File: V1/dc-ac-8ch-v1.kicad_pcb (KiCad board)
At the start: 2 copper layers, 98 x 67.8 mm, 103 parts, among them J1 DB142V-5.08-4P, J2 DB142V-5.08-4P, J3 DB142V-5.08-2P, J4 DB142V-5.08-4P, J5 DB142V-5.08-4P, J6 DB142V-5.08-2P, U1 MOC3063S, U2 MOC3063S, U3 MOC3063S, U4 MOC3063S, U5 MOC3063S, U6 MOC3063S, U7 MOC3063S, U8 MOC3063S

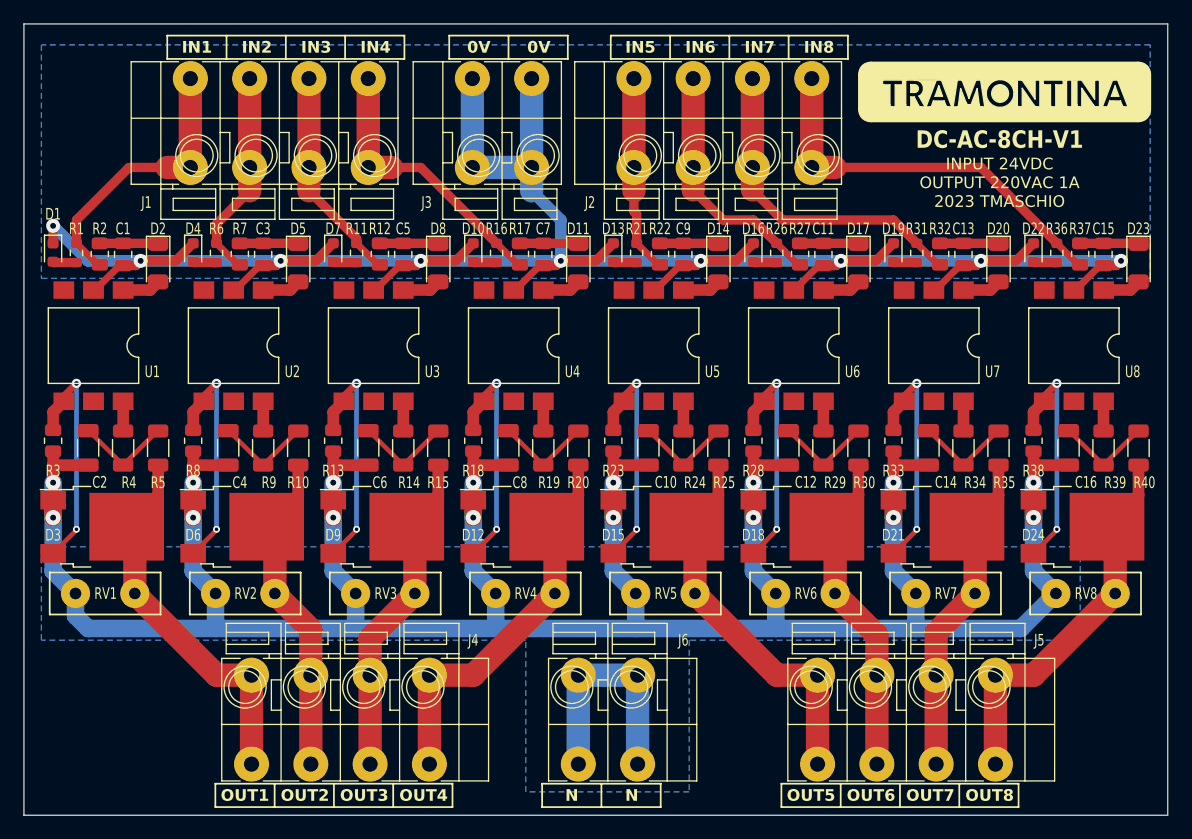
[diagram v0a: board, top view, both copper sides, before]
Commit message: Place missing track under zone
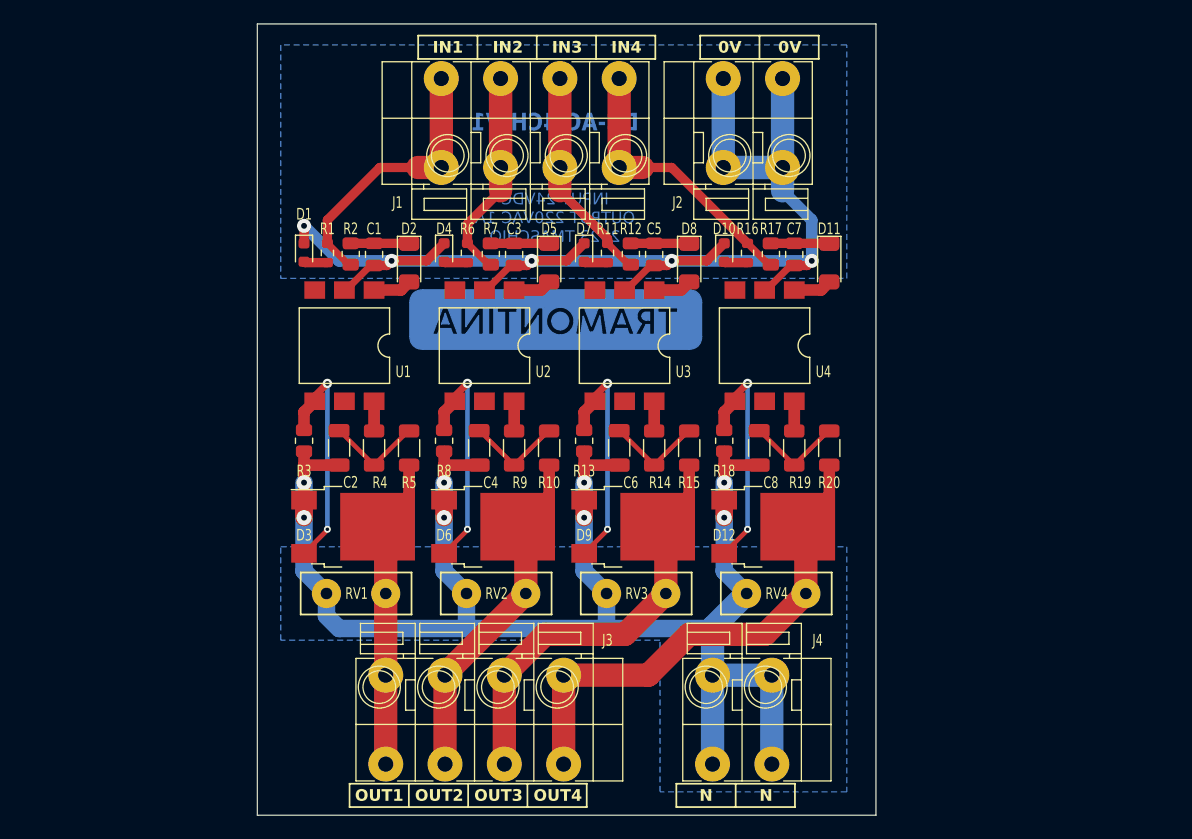
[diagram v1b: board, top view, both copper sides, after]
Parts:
- removed C10, C12, C14, C16: 22nF/630V, Tales:C_1206_3216Metric
- removed C11, C13, C15, C9: 33nF/50V, Tales:C_0805_2012Metric
- removed D13, D16, D19, D22: GREEN, Tales:LED_0603_1608Metric
- removed D14, D17, D20, D23: 9V1/500mW, Tales:D_SOD-123
- removed D15, D18, D21, D24: T435-600B, Tales:TO-252-2
- removed the J2 at (167.5, 66.9)
- removed J5: DB142V-5.08-4P, Tales:TerminalBlock_Dibo_DB142V-5.08-4P_1x04_P5.08mm_Vertical
- removed R21, R26, R31, R36: 5,6k/100mW, Tales:R_0603_1608Metric
- removed R22, R27, R32, R37: 1k8/125mW, Tales:R_0805_2012Metric
- removed R23, R28, R33, R38: 390R/125mW, Tales:R_0805_2012Metric
- removed R24, R29, R34, R39: 150R/250mW, Tales:R_1206_3216Metric
- removed R25, R30, R35, R40: 51R/250mW, Tales:R_1206_3216Metric
- removed the REF** at (184.1, 68.0)
- removed RV5, RV6, RV7, RV8: 275VAC, Tales:RV_Disc_D9.50mm_W3.6mm_P5.08mm
- removed U5, U6, U7, U8: MOC3063S, Tales:SMDIP-6_W9.53mm_Clearance8mm
- added REF**: Logo_Tramontina_25mm_Silk, Tales:Logo_Tramontina_25mm_Bottom, F.Cu at (145.5, 87.5)
- moved U2 21.5 mm to (139.5, 89.8)
- moved C1 21.5 mm to (130.0, 82.0)
- moved C2 21.5 mm to (127.0, 98.5)
- moved C3 21.5 mm to (142.0, 82.0)
- moved C4 21.5 mm to (139.0, 98.5)
- moved C5 21.5 mm to (154.0, 82.0)
- moved C6 21.5 mm to (151.0, 98.5)
- moved C7 21.5 mm to (166.0, 82.0)
- moved C8 21.5 mm to (163.0, 98.5)
- moved D1 21.5 mm to (124.0, 81.8)
- moved D10 21.5 mm to (160.0, 81.8)
- moved D11 21.5 mm to (169.0, 82.7)
- moved D12 21.5 mm to (164.2, 105.3)
- moved D2 21.5 mm to (133.0, 82.7)
- moved D4 21.5 mm to (136.0, 81.8)
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- renumbered J3 to J2, J4 to J3, J6 to J4
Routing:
- net NEUTRAL: track 277.7 -> 145.9 mm, vias 16 -> 8
- net GND: track 200.1 -> 111.3 mm, vias 9 -> 5
- net Net-(J2-Pin_1): track 34.1 -> 0.00 mm
- net Net-(D15-A2): track 33.4 -> 0.00 mm
- net Net-(D24-A2): track 33.2 -> 0.00 mm
- net Net-(D18-A2): track 28.5 -> 0.00 mm
- net Net-(D21-A2): track 28.4 -> 0.00 mm
- net Net-(J2-Pin_2): track 28.3 -> 0.00 mm
- net Net-(J2-Pin_3): track 21.4 -> 0.00 mm
- net Net-(D24-G): track 20.2 -> 0.00 mm, vias 2 -> 0
- net Net-(D21-G): track 20.2 -> 0.00 mm, vias 2 -> 0
- net Net-(D18-G): track 20.2 -> 0.00 mm, vias 2 -> 0
- net Net-(D15-G): track 20.2 -> 0.00 mm, vias 2 -> 0
- net Net-(J2-Pin_4): track 17.0 -> 0.00 mm
- net Net-(D12-A2): track 33.7 -> 43.7 mm
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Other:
- board size 98 x 67.8 mm -> 53 x 67.8 mm
- board text added: "DC-AC-4CH-V1"
- board text removed: "DC-AC-8CH-V1"
- board text removed: "IN5"
- board text removed: "IN6"
- board text removed: "IN7"
- board text removed: "IN8"
- board text removed: "OUT5"
- board text removed: "OUT6"
- board text removed: "OUT7"
- board text removed: "OUT8"
